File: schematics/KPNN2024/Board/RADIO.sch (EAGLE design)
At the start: 16 parts, among them J1 IPX-RADIO, J2 IPX-ANT

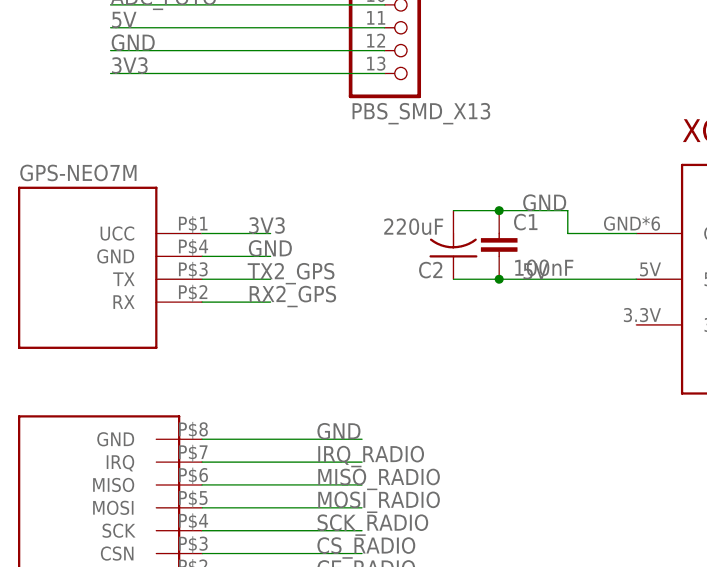
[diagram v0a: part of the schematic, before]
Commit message: поправила платы
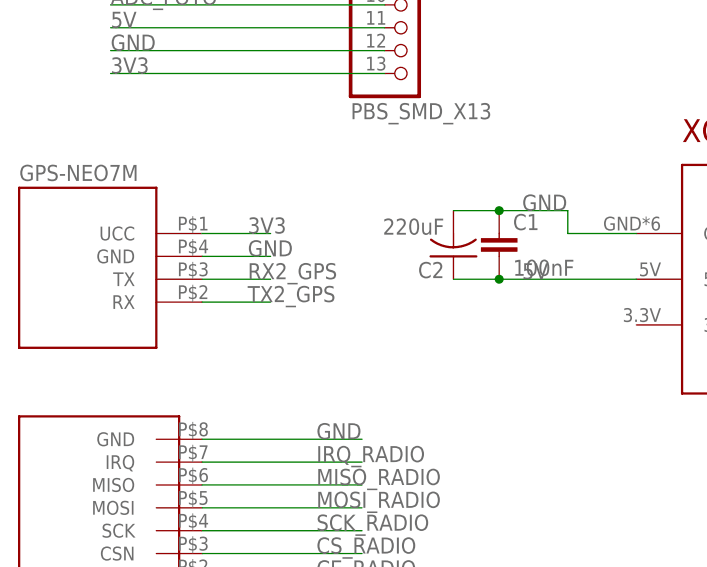
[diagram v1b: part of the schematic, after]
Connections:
- net RX2_GPS: now also GPS-NEO7M.TX; no longer GPS-NEO7M.RX
- net TX2_GPS: now also GPS-NEO7M.RX; no longer GPS-NEO7M.TX
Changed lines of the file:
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@@
 <layers>
 <layer number="1" name="Top" color="4" fill="1" visible="no" active="no"/>
+<layer number="2" name="Route2" color="16" fill="1" visible="no" active="no"/>
+<layer number="3" name="Route3" color="17" fill="1" visible="no" active="no"/>
+<layer number="4" name="Route4" color="18" fill="1" visible="no" active="no"/>
+<layer number="5" name="Route5" color="19" fill="1" visible="no" active="no"/>
+<layer number="6" name="Route6" color="25" fill="1" visible="no" active="no"/>
+<layer number="7" name="Route7" color="26" fill="1" visible="no" active="no"/>
+<layer number="8" name="Route8" color="27" fill="1" visible="no" active="no"/>
+<layer number="9" name="Route9" color="28" fill="1" visible="no" active="no"/>
+<layer number="10" name="Route10" color="29" fill="1" visible="no" active="no"/>
+<layer number="11" name="Route11" color="30" fill="1" visible="no" active="no"/>
+<layer number="12" name="Route12" color="20" fill="1" visible="no" active="no"/>
+<layer number="13" name="Route13" color="21" fill="1" visible="no" active="no"/>
+<layer number="14" name="Route14" color="22" fill="1" visible="no" active="no"/>
+<layer number="15" name="Route15" color="23" fill="1" visible="no" active="no"/>
 <layer number="16" name="Bottom" color="1" fill="1" visible="no" active="no"/>
 <layer number="17" name="Pads" color="2" fill="1" visible="no" active="no"/>
@@
 </segment>
 <segment>
+<pinref part="GPS-NEO7M" gate="G$1" pin="RX"/>
+<wire x1="20.32" y1="76.2" x2="27.94" y2="76.2" width="0.1524" layer="91"/>
+<label x="25.4" y="76.2" size="1.778" layer="95"/>
+</segment>
+</net>
+<net name="RX2_GPS" class="0">
+<segment>
+<wire x1="86.36" y1="114.3" x2="55.88" y2="114.3" width="0.1524" layer="91"/>
+<pinref part="U$7" gate="G$1" pin="8"/>
+<label x="55.88" y="114.3" size="1.778" layer="95"/>
+</segment>
+<segment>
 <pinref part="GPS-NEO7M" gate="G$1" pin="TX"/>
 <wire x1="20.32" y1="78.74" x2="27.94" y2="78.74" width="0.1524" layer="91"/>
@@
 </segment>
 </net>
-<net name="RX2_GPS" class="0">
-<segment>
-<wire x1="86.36" y1="114.3" x2="55.88" y2="114.3" width="0.1524" layer="91"/>
-<pinref part="U$7" gate="G$1" pin="8"/>
-<label x="55.88" y="114.3" size="1.778" layer="95"/>
-</segment>
-<segment>
-<pinref part="GPS-NEO7M" gate="G$1" pin="RX"/>
-<wire x1="20.32" y1="76.2" x2="27.94" y2="76.2" width="0.1524" layer="91"/>
-<label x="25.4" y="76.2" size="1.778" layer="95"/>
-</segment>
-</net>

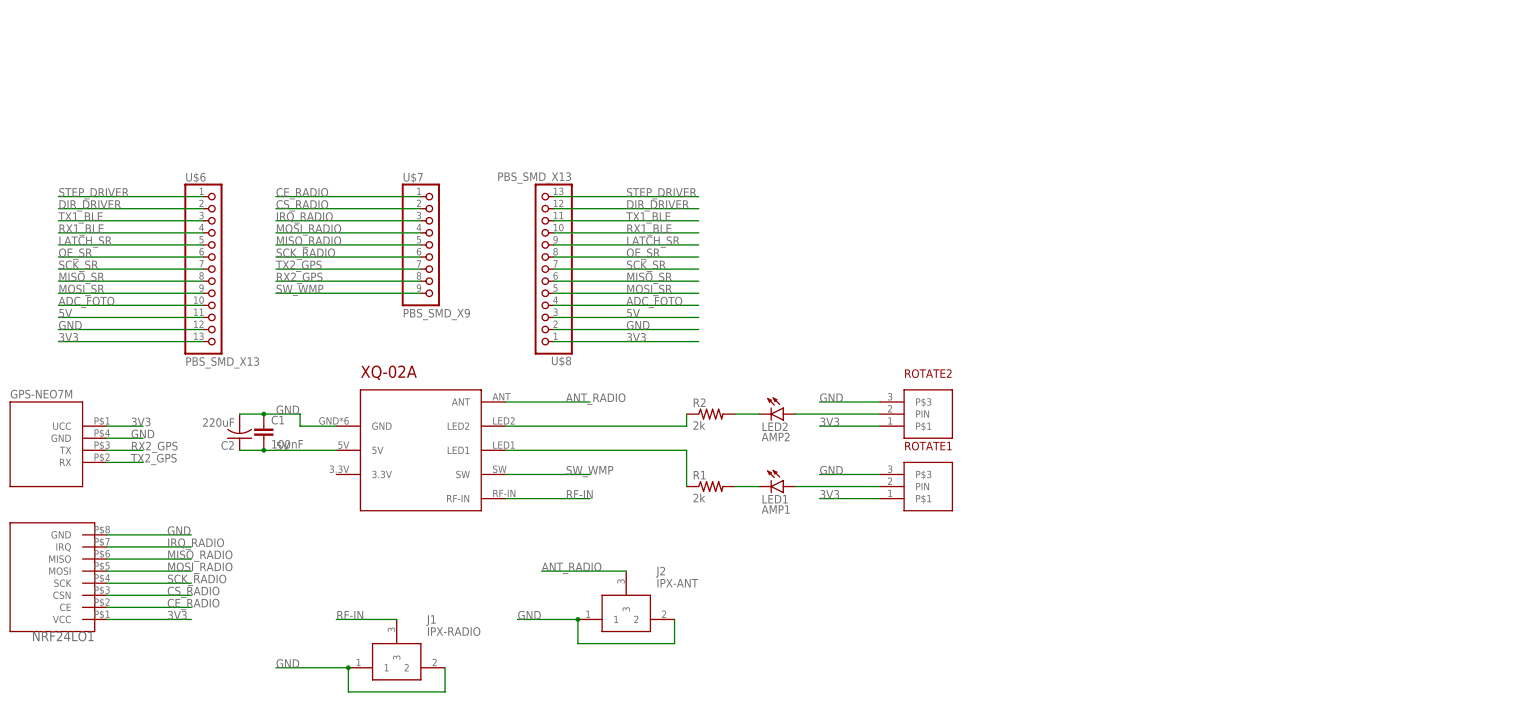
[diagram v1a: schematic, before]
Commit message: Модели поправлены в соответствии с платами
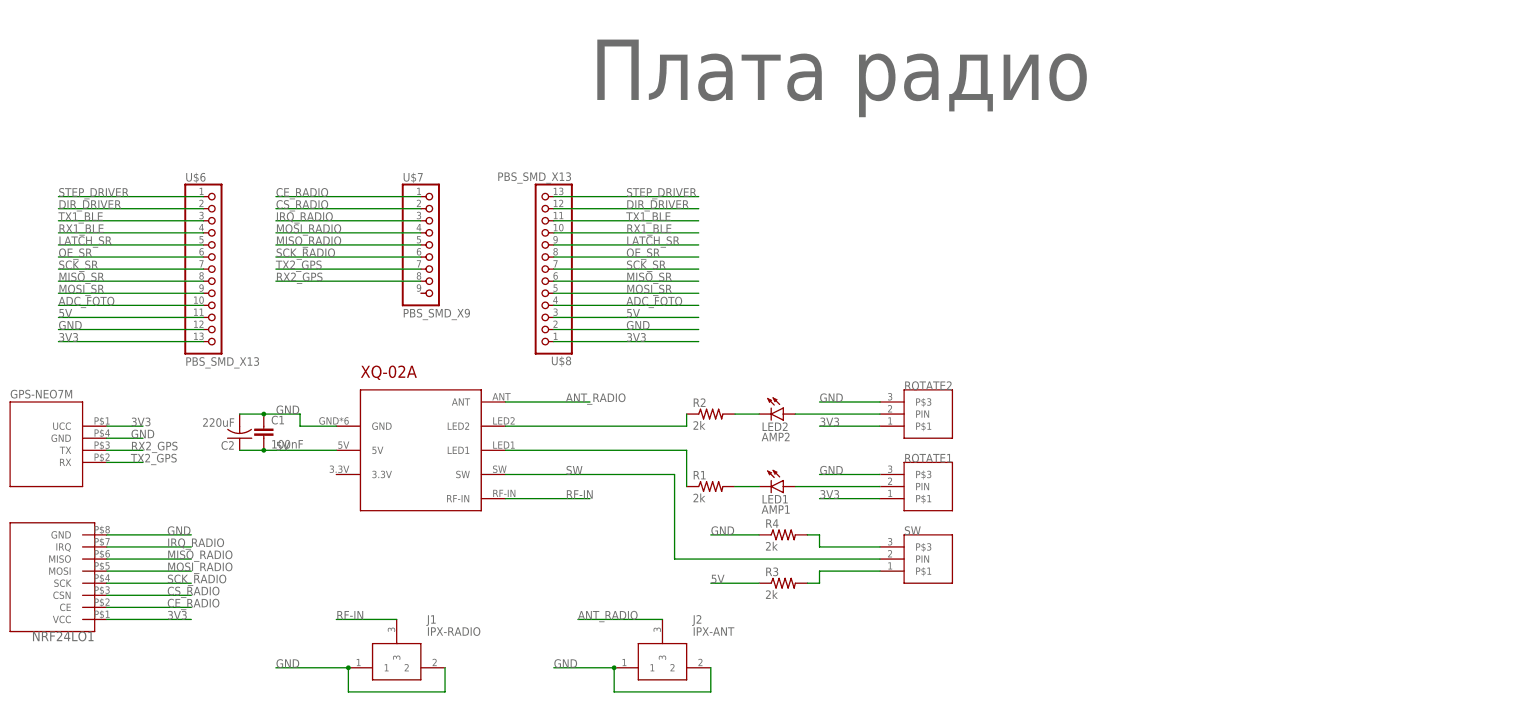
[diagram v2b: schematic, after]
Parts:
- added R3, R4: 2k, rcl:R-US_R0603
- added SW: CONNECT_3, UNKNOWN-2024:CONNECT_3
- added U$1: Плата радио, UNKNOWN-2024:LOGOPCB-""
- C2: device CanCubeSat:ECAPECAP220 -> UNKNOWN-2024:ECAPECAP220
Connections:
- removed net SW_WMP: U$7.9, XQ-02A.SW
- new net N$7: R3.2, SW.P$1
- new net N$8: R4.2, SW.P$3
- new net SW: SW.PIN, XQ-02A.SW
- net 5V: now also R3.1
- net GND: now also R4.1
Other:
- moved on the sheet: J2
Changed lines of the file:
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@@
 <part name="R2" library="rcl" library_urn="urn:adsk.eagle:library:334" deviceset="R-US_" device="R0603" package3d_urn="urn:adsk.eagle:package:23555/3" value="2k"/>
 <part name="C1" library="rcl" library_urn="urn:adsk.eagle:library:334" deviceset="C-EU" device="C0603" package3d_urn="urn:adsk.eagle:package:23616/2" value="100nF"/>
-<part name="C2" library="CanCubeSat" deviceset="ECAP" device="ECAP220" value="220uF"/>
+<part name="C2" library="UNKNOWN-2024" deviceset="ECAP" device="ECAP220" value="220uF"/>
+<part name="U$1" library="UNKNOWN-2024" deviceset="LOGO" device="PCB-&quot;&quot;" value="Плата радио"/>
+<part name="SW" library="UNKNOWN-2024" deviceset="CONNECT_3" device=""/>
+<part name="R3" library="rcl" library_urn="urn:adsk.eagle:library:334" deviceset="R-US_" device="R0603" package3d_urn="urn:adsk.eagle:package:23555/3" value="2k"/>
+<part name="R4" library="rcl" library_urn="urn:adsk.eagle:library:334" deviceset="R-US_" device="R0603" package3d_urn="urn:adsk.eagle:package:23555/3" value="2k"/>
 </parts>
 <sheets>
@@
 <attribute name="VALUE" x="87.63" y="40.64" size="1.778" layer="96" align="center-left"/>
 </instance>
-<instance part="J2" gate="G$1" x="119.38" y="43.18" smashed="yes">
-<attribute name="NAME" x="135.89" y="53.34" size="1.778" layer="95" align="center-left"/>
-<attribute name="VALUE" x="135.89" y="50.8" size="1.778" layer="96" align="center-left"/>
+<instance part="J2" gate="G$1" x="127" y="33.02" smashed="yes">
+<attribute name="NAME" x="143.51" y="43.18" size="1.778" layer="95" align="center-left"/>
+<attribute name="VALUE" x="143.51" y="40.64" size="1.778" layer="96" align="center-left"/>
 </instance>
 <instance part="ROTATE1" gate="G$1" x="187.96" y="71.12" smashed="yes">
-<attribute name="NAME" x="187.96" y="78.74" size="1.778" layer="94"/>
+<attribute name="NAME" x="187.96" y="76.2" size="1.778" layer="95"/>
 </instance>
 <instance part="ROTATE2" gate="G$1" x="187.96" y="86.36" smashed="yes">
-<attribute name="NAME" x="187.96" y="93.98" size="1.778" layer="94"/>
+<attribute name="NAME" x="187.96" y="91.44" size="1.778" layer="95"/>
 </instance>
 <instance part="U$6" gate="G$1" x="43.18" y="116.84" smashed="yes">
@@
 <attribute name="NAME" x="47.244" y="80.645" size="1.778" layer="95" rot="R180"/>
 <attribute name="VALUE" x="47.244" y="85.471" size="1.778" layer="96" rot="R180"/>
+</instance>
+<instance part="U$1" gate="G$1" x="17.78" y="152.4" smashed="yes">
+<attribute name="VALUE" x="121.92" y="152.4" size="12.7" layer="96"/>
+</instance>
+<instance part="SW" gate="G$1" x="187.96" y="55.88" smashed="yes">
+<attribute name="NAME" x="187.96" y="60.96" size="1.778" layer="95"/>
+</instance>
+<instance part="R3" gate="G$1" x="162.56" y="50.8" smashed="yes">
+<attribute name="NAME" x="158.75" y="52.2986" size="1.778" layer="95"/>
+<attribute name="VALUE" x="158.75" y="47.498" size="1.778" layer="96"/>
+</instance>
+<instance part="R4" gate="G$1" x="162.56" y="60.96" smashed="yes">
+<attribute name="NAME" x="158.75" y="62.4586" size="1.778" layer="95"/>
+<attribute name="VALUE" x="158.75" y="57.658" size="1.778" layer="96"/>
 </instance>
 </instances>
@@
 <segment>
 <pinref part="J2" gate="G$1" pin="2"/>
-<wire x1="139.7" y1="43.18" x2="139.7" y2="38.1" width="0.1524" layer="91"/>
-<wire x1="139.7" y1="38.1" x2="119.38" y2="38.1" width="0.1524" layer="91"/>
+<wire x1="147.32" y1="33.02" x2="147.32" y2="27.94" width="0.1524" layer="91"/>
+<wire x1="147.32" y1="27.94" x2="127" y2="27.94" width="0.1524" layer="91"/>
 <pinref part="J2" gate="G$1" pin="1"/>
-<wire x1="119.38" y1="38.1" x2="119.38" y2="43.18" width="0.1524" layer="91"/>
-<wire x1="119.38" y1="43.18" x2="106.68" y2="43.18" width="0.1524" layer="91"/>
-<junction x="119.38" y="43.18"/>
-<label x="106.68" y="43.18" size="1.778" layer="95"/>
+<wire x1="127" y1="27.94" x2="127" y2="33.02" width="0.1524" layer="91"/>
+<wire x1="127" y1="33.02" x2="114.3" y2="33.02" width="0.1524" layer="91"/>
+<junction x="127" y="33.02"/>
+<label x="114.3" y="33.02" size="1.778" layer="95"/>
 </segment>
 <segment>
@@
 <label x="129.54" y="104.14" size="1.778" layer="95"/>
 <pinref part="U$8" gate="G$1" pin="2"/>
+</segment>
+<segment>
+<pinref part="R4" gate="G$1" pin="1"/>
+<wire x1="157.48" y1="60.96" x2="147.32" y2="60.96" width="0.1524" layer="91"/>
+<label x="147.32" y="60.96" size="1.778" layer="95"/>
 </segment>
 </net>
@@
 <pinref part="U$8" gate="G$1" pin="3"/>
 </segment>
+<segment>
+<pinref part="R3" gate="G$1" pin="1"/>
+<wire x1="157.48" y1="50.8" x2="147.32" y2="50.8" width="0.1524" layer="91"/>
+<label x="147.32" y="50.8" size="1.778" layer="95"/>
+</segment>
 </net>
 <net name="RF-IN" class="0">
@@
 <segment>
 <pinref part="J2" gate="G$1" pin="3"/>
-<wire x1="129.54" y1="53.34" x2="111.76" y2="53.34" width="0.1524" layer="91"/>
-<label x="111.76" y="53.34" size="1.778" layer="95"/>
+<wire x1="137.16" y1="43.18" x2="119.38" y2="43.18" width="0.1524" layer="91"/>
+<label x="119.38" y="43.18" size="1.778" layer="95"/>
 </segment>
 <segment>
@@
 </segment>
 </net>
-<net name="SW_WMP" class="0">
-<segment>
-<wire x1="86.36" y1="111.76" x2="55.88" y2="111.76" width="0.1524" layer="91"/>
-<pinref part="U$7" gate="G$1" pin="9"/>
-<label x="55.88" y="111.76" size="1.778" layer="95"/>
-</segment>
+<net name="SW" class="0">
 <segment>
 <pinref part="XQ-02A" gate="G$1" pin="SW"/>
-<wire x1="104.14" y1="73.66" x2="121.92" y2="73.66" width="0.1524" layer="91"/>
+<wire x1="104.14" y1="73.66" x2="139.7" y2="73.66" width="0.1524" layer="91"/>
+<wire x1="139.7" y1="73.66" x2="139.7" y2="55.88" width="0.1524" layer="91"/>
+<pinref part="SW" gate="G$1" pin="PIN"/>
+<wire x1="139.7" y1="55.88" x2="182.88" y2="55.88" width="0.1524" layer="91"/>
 <label x="116.84" y="73.66" size="1.778" layer="95"/>
 </segment>
@@
 </segment>
 </net>
+<net name="N$7" class="0">
+<segment>
+<pinref part="SW" gate="G$1" pin="P$1"/>
+<wire x1="182.88" y1="53.34" x2="170.18" y2="53.34" width="0.1524" layer="91"/>
+<pinref part="R3" gate="G$1" pin="2"/>
+<wire x1="167.64" y1="50.8" x2="170.18" y2="50.8" width="0.1524" layer="91"/>
+<wire x1="170.18" y1="50.8" x2="170.18" y2="53.34" width="0.1524" layer="91"/>
+</segment>
+</net>
+<net name="N$8" class="0">
+<segment>
+<wire x1="182.88" y1="58.42" x2="170.18" y2="58.42" width="0.1524" layer="91"/>
+<pinref part="R4" gate="G$1" pin="2"/>
+<wire x1="167.64" y1="60.96" x2="170.18" y2="60.96" width="0.1524" layer="91"/>
+<wire x1="170.18" y1="60.96" x2="170.18" y2="58.42" width="0.1524" layer="91"/>
+<pinref part="SW" gate="G$1" pin="P$3"/>
+</segment>
+</net>
